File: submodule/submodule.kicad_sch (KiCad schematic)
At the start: 1 part, among them U1 ADS1299IPAG

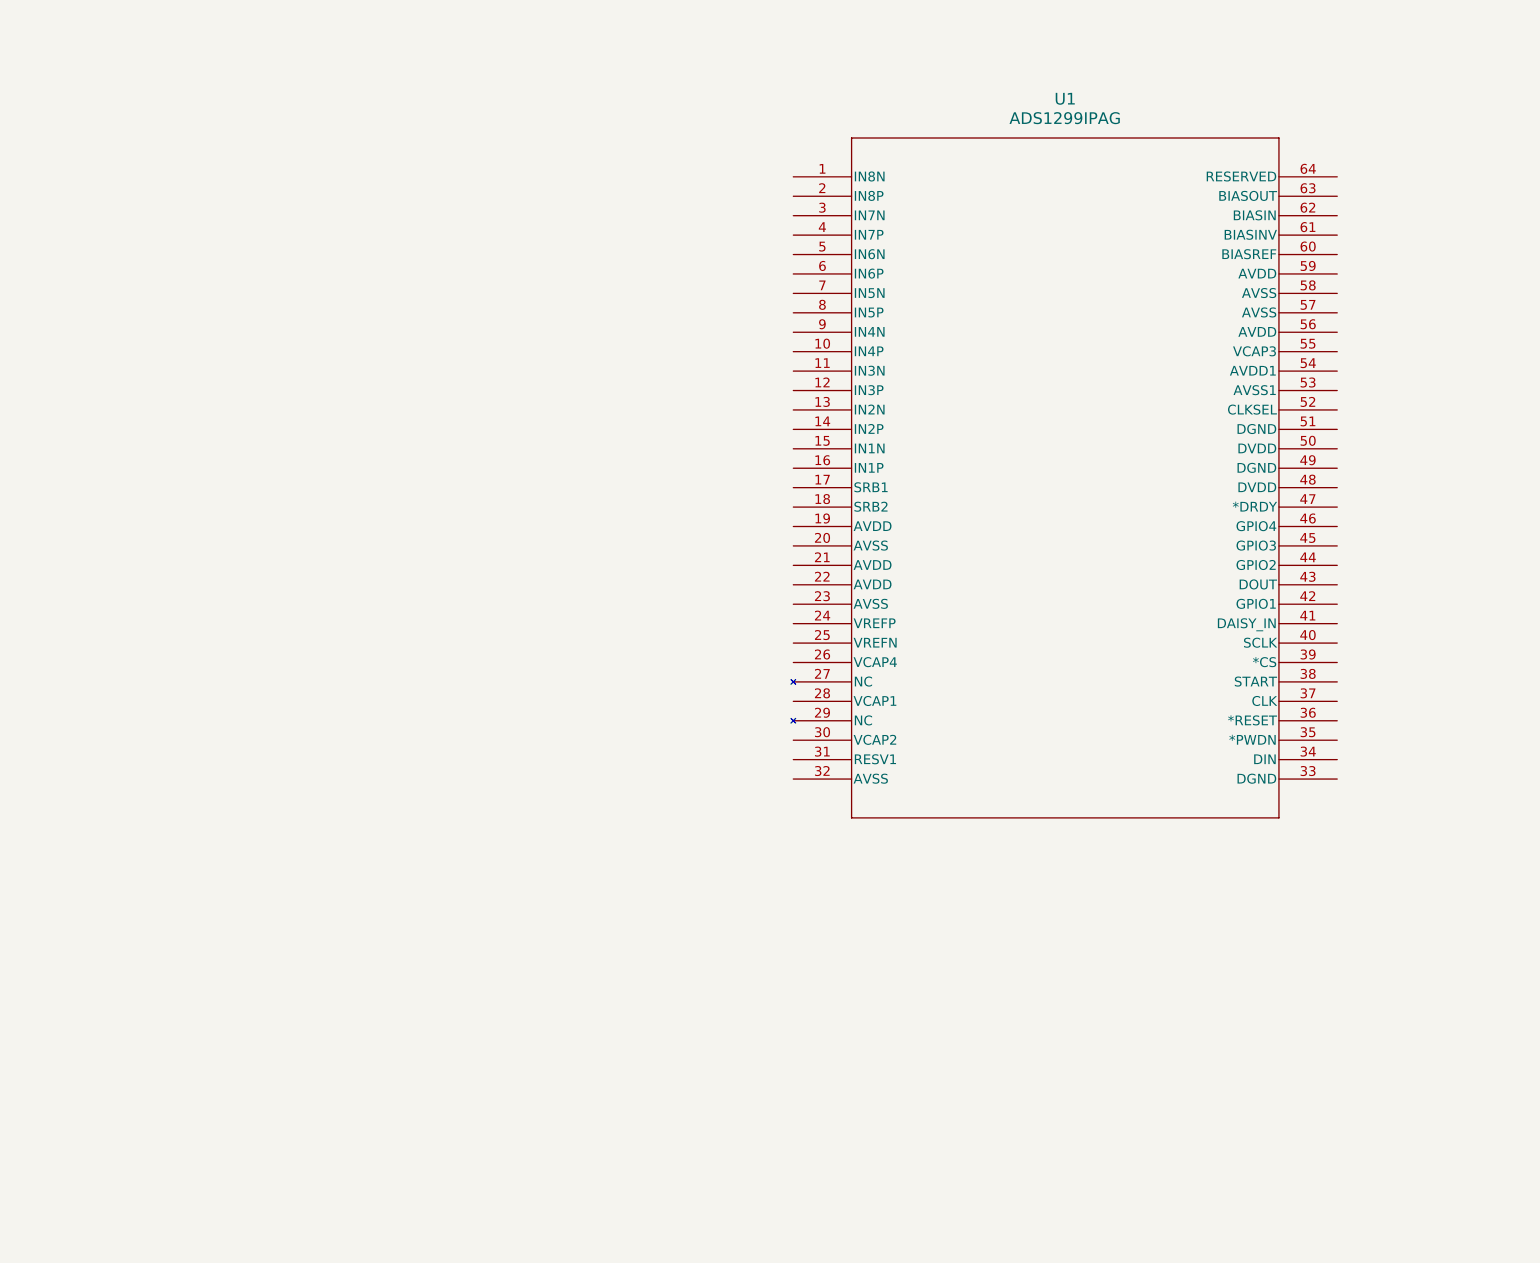
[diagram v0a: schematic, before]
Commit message: Conexiones SPI
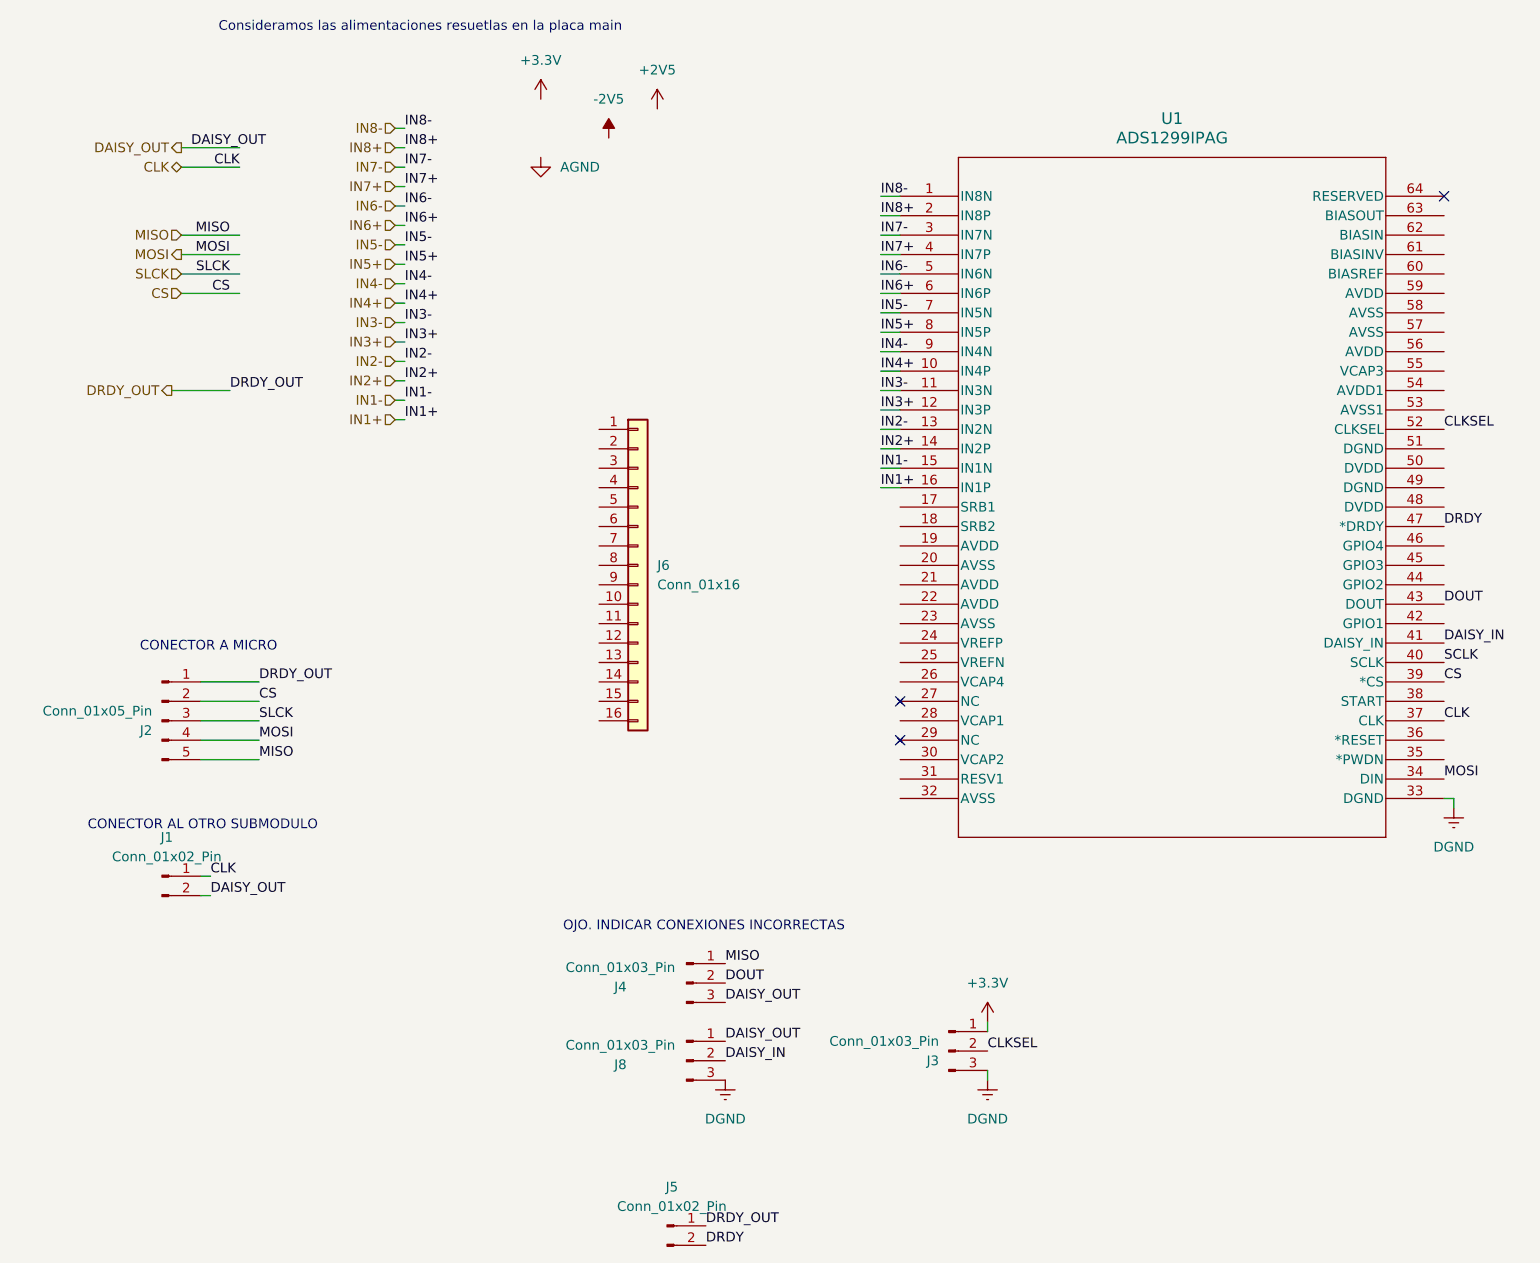
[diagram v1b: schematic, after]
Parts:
- added J1, J5: Conn_01x02_Pin, symbol Connector:Conn_01x02_Pin
- added J2: Conn_01x05_Pin, symbol Connector:Conn_01x05_Pin
- added J3, J4, J8: Conn_01x03_Pin, symbol Connector:Conn_01x03_Pin
- added J6: Conn_01x16, symbol Connector_Generic:Conn_01x16
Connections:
- net IN8-: now reaches U1.1 (IN8N)
- net IN4+: now reaches U1.10 (IN4P)
- net IN3-: now reaches U1.11 (IN3N)
- net IN3+: now reaches U1.12 (IN3P)
- net IN2-: now reaches U1.13 (IN2N)
- net IN2+: now reaches U1.14 (IN2P)
- net IN1-: now reaches U1.15 (IN1N)
- net IN1+: now reaches U1.16 (IN1P)
- net IN8+: now reaches U1.2 (IN8P)
- net IN7-: now reaches U1.3 (IN7N)
- net DGND: now reaches U1.33 (DGND)
- net DGND: now also J3.3 (Pin_3), J8.3 (Pin_3)
- net MOSI: now reaches U1.34 (DIN)
- net MOSI: now also J2.4 (Pin_4)
- net CLK: now reaches U1.37 (CLK)
- net CLK: now also J1.1 (Pin_1)
- net CS: now reaches U1.39 (*CS)
- net CS: now also J2.2 (Pin_2)
- net IN7+: now reaches U1.4 (IN7P)
- net SCLK: now reaches U1.40 (SCLK)
- net DAISY_IN: now reaches U1.41 (DAISY_IN)
- net DAISY_IN: now also J8.2 (Pin_2)
- net DOUT: now reaches U1.43 (DOUT)
- net DOUT: now also J4.2 (Pin_2)
- net DRDY: now reaches U1.47 (*DRDY)
- net DRDY: now also J5.2 (Pin_2)
- net IN6-: now reaches U1.5 (IN6N)
- net CLKSEL: now reaches U1.52 (CLKSEL)
- net CLKSEL: now also J3.2 (Pin_2)
- net IN6+: now reaches U1.6 (IN6P)
- net IN5-: now reaches U1.7 (IN5N)
- net IN5+: now reaches U1.8 (IN5P)
- net IN4-: now reaches U1.9 (IN4N)
- new net +3.3V: J3.1 (Pin_1)
- new net DAISY_OUT: J1.2 (Pin_2), J4.3 (Pin_3), J8.1 (Pin_1)
- new net DRDY_OUT: J2.1 (Pin_1), J5.1 (Pin_1)
- new net MISO: J2.5 (Pin_5), J4.1 (Pin_1)
- new net SLCK: J2.3 (Pin_3)
- no-connect marks 0 -> 3
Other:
- note added: "CONECTOR A MICRO"
- note added: "CONECTOR AL OTRO SUBMODULO"
- note added: "Consideramos las alimentaciones resuetlas en la placa main"
- note added: "OJO. INDICAR CONEXIONES INCORRECTAS"
- moved on the sheet: U1
